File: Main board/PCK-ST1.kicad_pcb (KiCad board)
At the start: 4 copper layers, 68.5 x 55.6 mm, 186 parts, among them IC1 DRV8434, IC2 DRV8434, IC3 DRV8434, IC4 DRV8434, IC5 TLV70033DDCR, IC7 TPS2121RUXR, IC8 TPS25730DREFR, J1 Conn_02x20_Odd_Even, J10 RA, J11 EL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

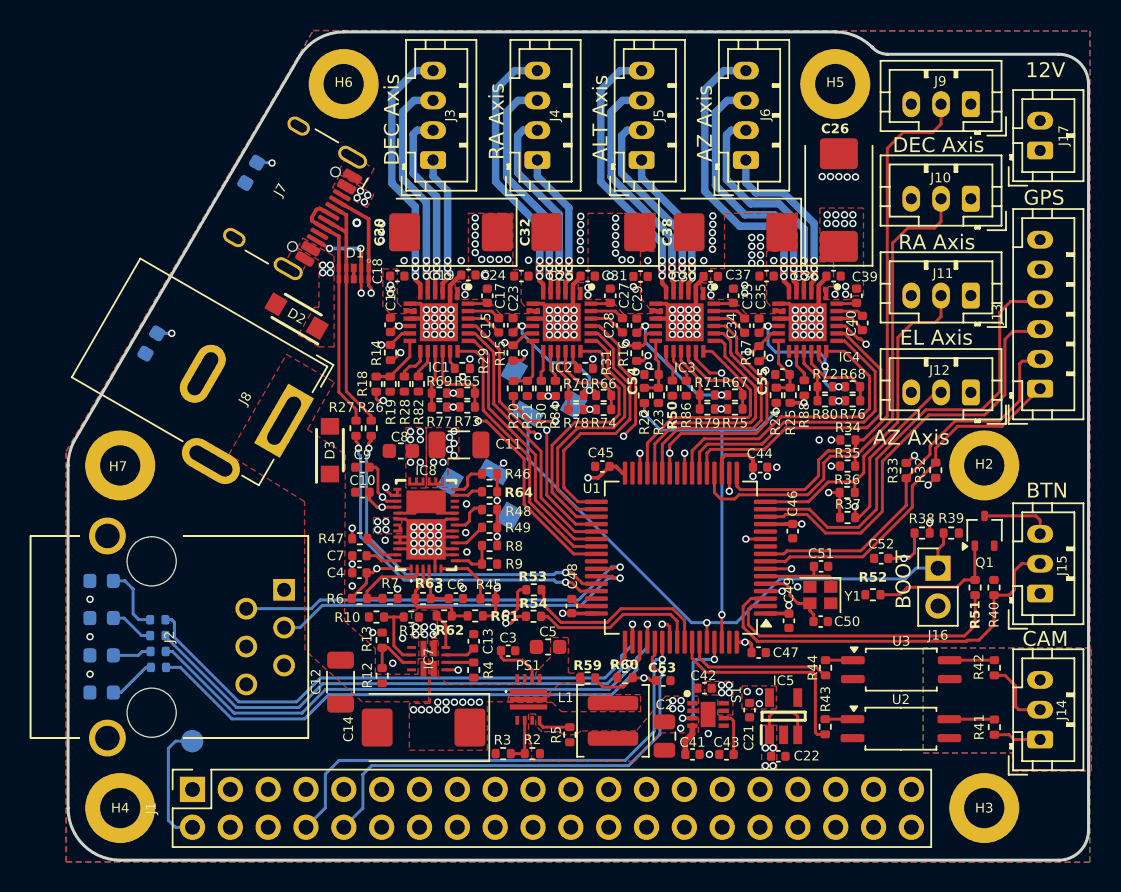
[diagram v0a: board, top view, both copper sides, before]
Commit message: Main board updated to v0.3
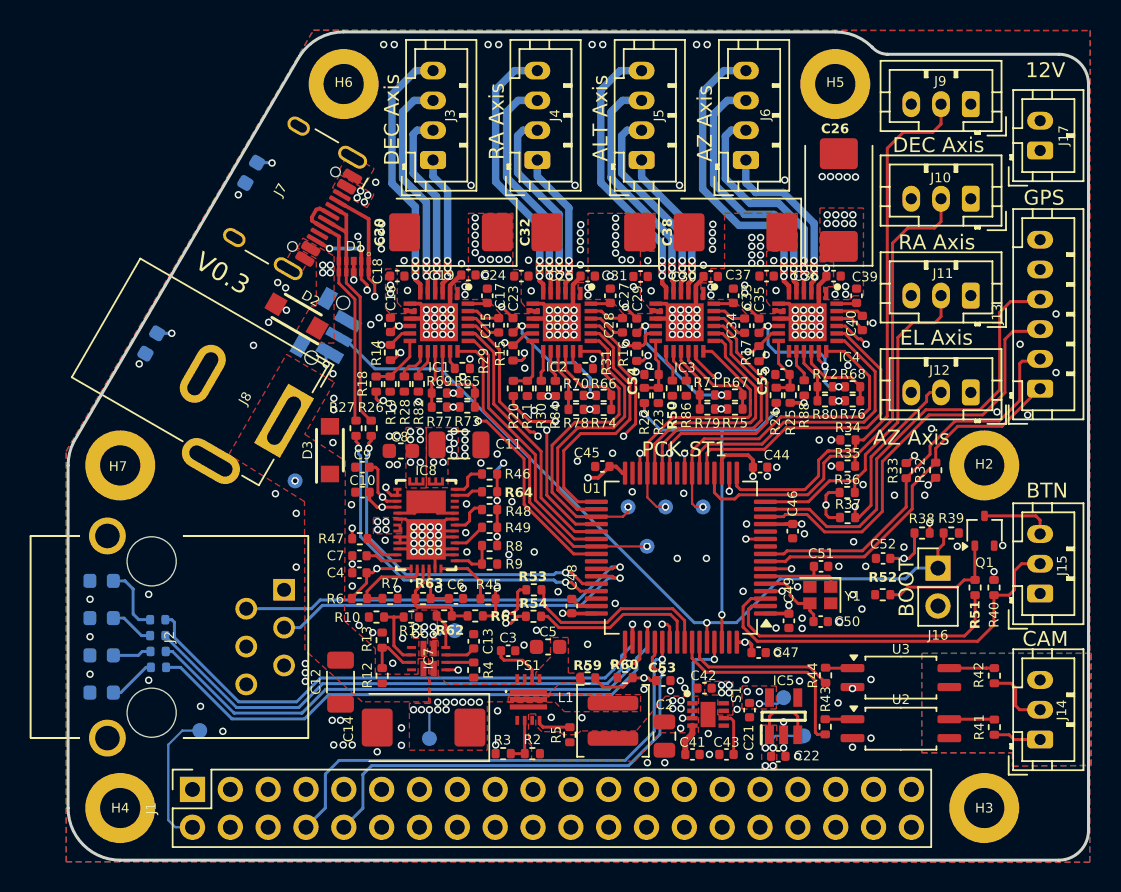
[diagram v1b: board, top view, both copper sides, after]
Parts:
- added TP1: TestPoint, TestPoint:TestPoint_Pad_D1.0mm, B.Cu at (141.8, 106.8)
- added TP10: TestPoint, TestPoint:TestPoint_Pad_D1.0mm, B.Cu at (160.1, 91.3)
- added TP2: TestPoint, TestPoint:TestPoint_Pad_D1.0mm, B.Cu at (166.9, 106.7)
- added TP3: TestPoint, TestPoint:TestPoint_Pad_D1.0mm, B.Cu at (165.5, 104.1)
- added TP5: TestPoint, TestPoint:TestPoint_Pad_D1.0mm, B.Cu at (143.5, 99.6)
- added TP6: TestPoint, TestPoint:TestPoint_Pad_D1.0mm, B.Cu at (132.7, 89.5)
- added TP7: TestPoint, TestPoint:TestPoint_Pad_D1.0mm, B.Cu at (156.4, 93.9)
- added TP8: TestPoint, TestPoint:TestPoint_Pad_D1.0mm, B.Cu at (155.1, 91.3)
- added TP9: TestPoint, TestPoint:TestPoint_Pad_D1.0mm, B.Cu at (157.6, 91.3)
- R19, R21, R23: value 22k -> 10k
- R22: value 28k -> 20k
- R24: value 39k -> 47k
- R25: value 11k -> 10k
- SW1: footprint SamacSys_Parts.pretty:TL3336AF160Q -> SamacSys_Parts.pretty:SKRTLAE010
- TP4: footprint TestPoint:TestPoint_Pad_D1.5mm -> TestPoint:TestPoint_Pad_D1.0mm
- moved SW1 11.3 mm to (134.6, 79.2), turned to 60 degrees
- moved TP4 0.87 mm to (126.3, 106.3)
- moved R52 0.66 mm to (172.2, 97.2)
- moved U3 0.53 mm to (173.4, 102.7)
- moved R42 0.53 mm to (179.7, 102.6)
- moved R44 0.51 mm to (168.4, 102.6)
- moved D1 0.46 mm to (136.7, 75.2)
- moved C52 0.13 mm to (172.2, 94.7)
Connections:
- net /STEP_n_SLEEP renamed /ALT Stepper driver/nSLEEP
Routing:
- net /MCU/BOOT: track 40.4 -> 53.5 mm
- net /DEC Stepper driver/STEP: track 18.6 -> 22.0 mm, vias 0 -> 1
- net +3V3: track 26.4 -> 29.8 mm, vias 20 -> 21
- net /ALT Stepper driver/STEP: track 15.6 -> 18.8 mm, vias 0 -> 1
- net GND: track 67.5 -> 70.6 mm, vias 144 -> 278
- net /AZ Stepper driver/STEP: track 20.3 -> 23.2 mm, vias 0 -> 1
- net +5V: track 6.70 -> 9.47 mm
- net /MCU/RA_STEP: track 18.2 -> 20.8 mm, vias 0 -> 1
- net +12V: track 14.9 -> 16.8 mm
- net Net-(D5-A): track 42.0 -> 40.2 mm
- net /Power/VIN_USB: track 0.00 -> 1.55 mm
- net Net-(D4-A): track 48.0 -> 46.8 mm
- net /MCU/RPI_5V: track 8.44 -> 9.39 mm
- net /RA Stepper driver/DVDD: track 17.7 -> 16.8 mm
- net Net-(Q1-G): track 9.07 -> 8.40 mm
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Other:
- board text added: "PCK-ST1"
- board text added: "V0.3"
- board text added: "V0.3 2026-01-10"
- board text removed: "version 0.3 2025-12-02"

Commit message: Main board updated to v0.3
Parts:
- moved R8 0.10 mm to (145.8, 94.0)
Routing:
- net Net-(IC8-DRAIN_1): vias 0 -> 8
- net GND: vias 278 -> 281
- net /Power/VIN_USB: vias 13 -> 12
- added copper zone on B.Cu, net Net-(IC8-DRAIN_1)
- added copper zone on F.Cu, net Net-(IC8-DRAIN_1)
- added copper zone on In1.Cu, net Net-(IC8-DRAIN_1)
- added copper zone on In2.Cu, net Net-(IC8-DRAIN_1)

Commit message: Main board v0.3 to be manufactured
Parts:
- moved R13 0.28 mm to (138.6, 100.5)
- moved R43 0.13 mm to (168.5, 106.0)
- moved R26 0.10 mm to (137.7, 86.0)
- moved R44 0.10 mm to (168.5, 102.6)
- moved C14 0.08 mm to (141.4, 106.2)
- moved R27 0.08 mm to (136.8, 86.0)
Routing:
- net GND: track 70.6 -> 70.5 mm, vias 281 -> 300
- net /MCU/CAM_GND: vias 0 -> 7
- net +12V: vias 59 -> 62
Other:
- board text added: "V0.3 2026-01-18"
- board text removed: "V0.3 2026-01-10"

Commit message: Updated Main board to v1.0
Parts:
- removed J16: BOOT, Connector_PinHeader_2.54mm:PinHeader_1x02_P2.54mm_Vertical
- added REF**: ESD-Logo_6.6x6mm_SilkScreen, Symbol:ESD-Logo_6.6x6mm_SilkScreen, F.Cu at (174.0, 89.7)
- C15, C28, C34, C40: value 22nF/16V -> 22nF
- C16, C21, C22, C23, C29, C35, C41: value 1u/6.3V -> 1uF
- C17, C27, C33, C39: value 220nF/16V -> 220nF
- C18, C19, C24, C25, C30, C31, C36, C37: value 10nF/16V -> 10nF
- C2: value 22uF/16V -> 22uF/25V
- C42: value 100n/6.3V -> 100n
- C43: value 1n/6.3V -> 1n
- IC1, IC2, IC3, IC4: value DRV8434 -> DRV8434/24
- J1: value Conn_02x20_Odd_Even -> RPi; footprint Connector_PinSocket_2.54mm:PinSocket_2x20_P2.54mm_Vertical -> Connector_JST:JST_PH_B4B-PH-K_1x04_P2.00mm_Vertical
- moved J13 54.7 mm to (136.0, 111.8), turned to 0 degrees
- moved J17 54.4 mm to (151.2, 111.8), turned to 0 degrees
- moved R32 44.6 mm to (136.0, 109.0), turned to 180 degrees
- moved R33 42.4 mm to (136.0, 108.1), turned to 180 degrees
- moved J1 32.7 mm to (158.5, 111.8), turned to 0 degrees
- moved TP4 30.0 mm to (155.9, 111.7)
- moved J14 13.9 mm to (169.8, 111.8), turned to 0 degrees
- moved R41 8.41 mm to (171.7, 108.6)
- moved J15 7.92 mm to (178.5, 103.8)
- moved R44 7.32 mm to (175.8, 102.5)
- moved R39 7.17 mm to (171.9, 98.2)
- moved R42 7.15 mm to (175.7, 108.6)
- moved R43 4.82 mm to (171.7, 102.5)
- moved R40 4.18 mm to (175.8, 98.3)
- moved R52 3.94 mm to (176.0, 96.1)
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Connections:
- net /MCU/CAM_SHT renamed /MCU/CAM_SHTR
- J1 pad 1: unconnected-(J1-Pin_1-Pad1) -> /MCU/RPI_5V
- J1 pad 2: /MCU/RPI_5V -> /MCU/RPI_TX0
- J1 pad 3: unconnected-(J1-Pin_3-Pad3) -> /MCU/RPI_RX0
- J1 pad 4: /MCU/RPI_5V -> GND
- R29 pad 1: GND -> /DEC Stepper driver/DVDD
- R31 pad 1: GND -> /RA Stepper driver/DVDD
- U1 pad 58: /MCU/SHUTTER -> /MCU/FOCUS
- U1 pad 59: /MCU/FOCUS -> /MCU/SHUTTER
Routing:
- net /MCU/SCL_MAG: track 24.6 -> 43.5 mm, vias 0 -> 1
- net /MCU/RPI_TX0: track 33.8 -> 15.2 mm
- net /MCU/SDA_MAG: track 26.7 -> 43.4 mm, vias 0 -> 1
- net /MCU/RPI_RX0: track 32.0 -> 15.8 mm
- net /MCU/RX_GPS: track 28.6 -> 39.3 mm, vias 0 -> 1
- net /MCU/FOCUS: track 10.3 -> 19.3 mm
- net /MCU/BOOT: track 53.5 -> 45.3 mm, vias 1 -> 2
- net /MCU/TX_GPS: track 30.2 -> 37.7 mm, vias 0 -> 1
- net /MCU/RPI_5V: track 9.39 -> 2.63 mm
- net /MCU/PWR_BTN: track 27.5 -> 22.4 mm
- net Net-(Q1-G): track 8.38 -> 3.79 mm
- net +12V: track 16.8 -> 13.4 mm
- net Net-(U1-NRST): track 12.7 -> 9.73 mm
- net /DEC Stepper driver/DVDD: track 17.7 -> 20.1 mm, vias 3 -> 4
- net /MCU/IREG: track 25.5 -> 27.9 mm
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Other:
- board size 68.5 x 55.6 mm -> 65 x 55.6 mm
- board text added: "RPi UART"
- board text added: "V1.0 2026-02-14"
- board text added: "VIN"
- board text removed: "12V"
- board text removed: "BOOT"
- board text removed: "V0.3"
- board text removed: "V0.3 2026-01-18"
